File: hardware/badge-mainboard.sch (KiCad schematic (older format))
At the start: 0 parts

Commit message: splitted parts into connected schematic sheets
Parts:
- added C? (x2): 100nF, symbol C
- added C? (x3): 100nF, symbol C_Small
- added C?: 47uF, symbol C_Small
- added C?: 1uF, symbol C_Small
- added LED? (x3): WS2812b, WS2812B_1, symbol WS2812b
- added R? (x4): 10k, symbol R_Small
- added SW?: RESET-BTN, symbol SW_Push
- added U?: NINA-W102, symbol NINA-W102
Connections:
- net labels added: +1V8, +3.3V, +3V3, DTR, GND, NINA_SCL, NINA_SDA, RTS, RXD, TXD
- wire segments 0 -> 76
- no-connect marks 0 -> 1
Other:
- note added: "3 x RGBW LED Daisychain"
- note added: "Only one needed?\nVCC and VCC_IO are same in our case as we talk with 3.3v"
- note added: "Random I2C ports, any GPIO works."
- note added: "Random data port?"
- note added: "Which pullups? 10k or 200k?\nhttp://www.ti.com/lit/an/slva689/slva689.pdf"
- note added: "open drain buffers missing inthe picture for control signals (DTR & RTS)"

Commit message: Added NINA breakout module
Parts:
- removed C? (x2): 100nF, symbol C
- removed C?: 1uF, symbol C_Small
- removed R? (x2): 10k, symbol R_Small
- removed SW?: RESET-BTN, symbol SW_Push
- removed U?: NINA-W102, symbol NINA-W102
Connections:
- net labels removed: +3.3V, DTR, RTS
- wire segments 76 -> 52
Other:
- note added: "Random data port, can be changed if needed"
- note removed: "Only one needed?\nVCC and VCC_IO are same in our case as we talk with 3.3v"
- note removed: "Random data port?"
- note removed: "open drain buffers missing inthe picture for control signals (DTR & RTS)"

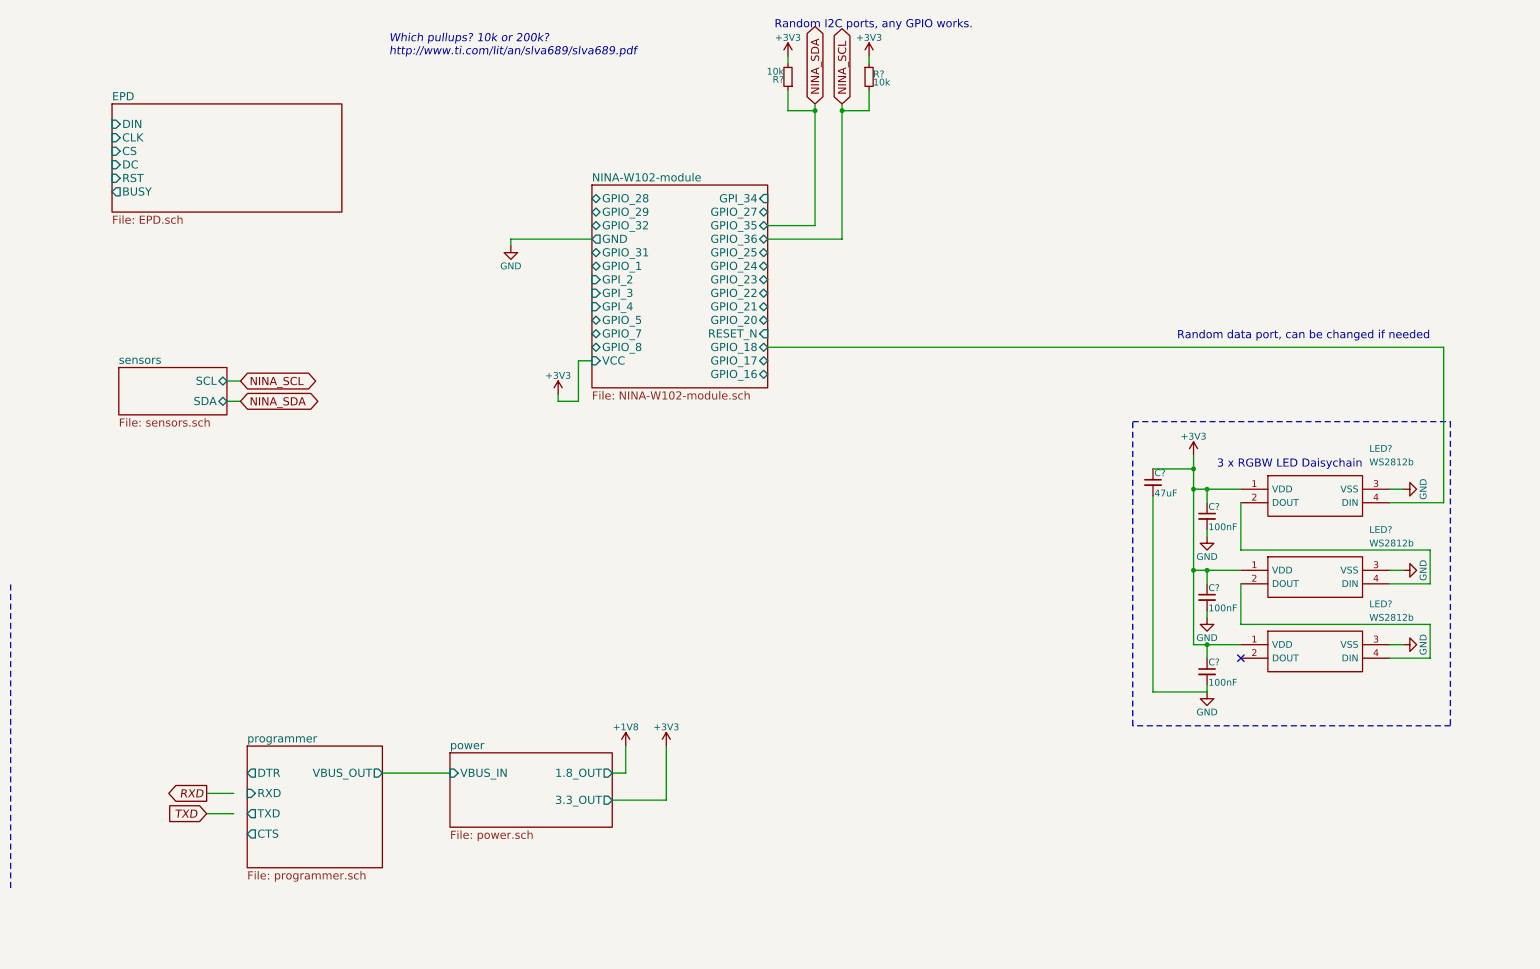
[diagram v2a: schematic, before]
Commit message: Added I2C headers and connected programmer to nina module
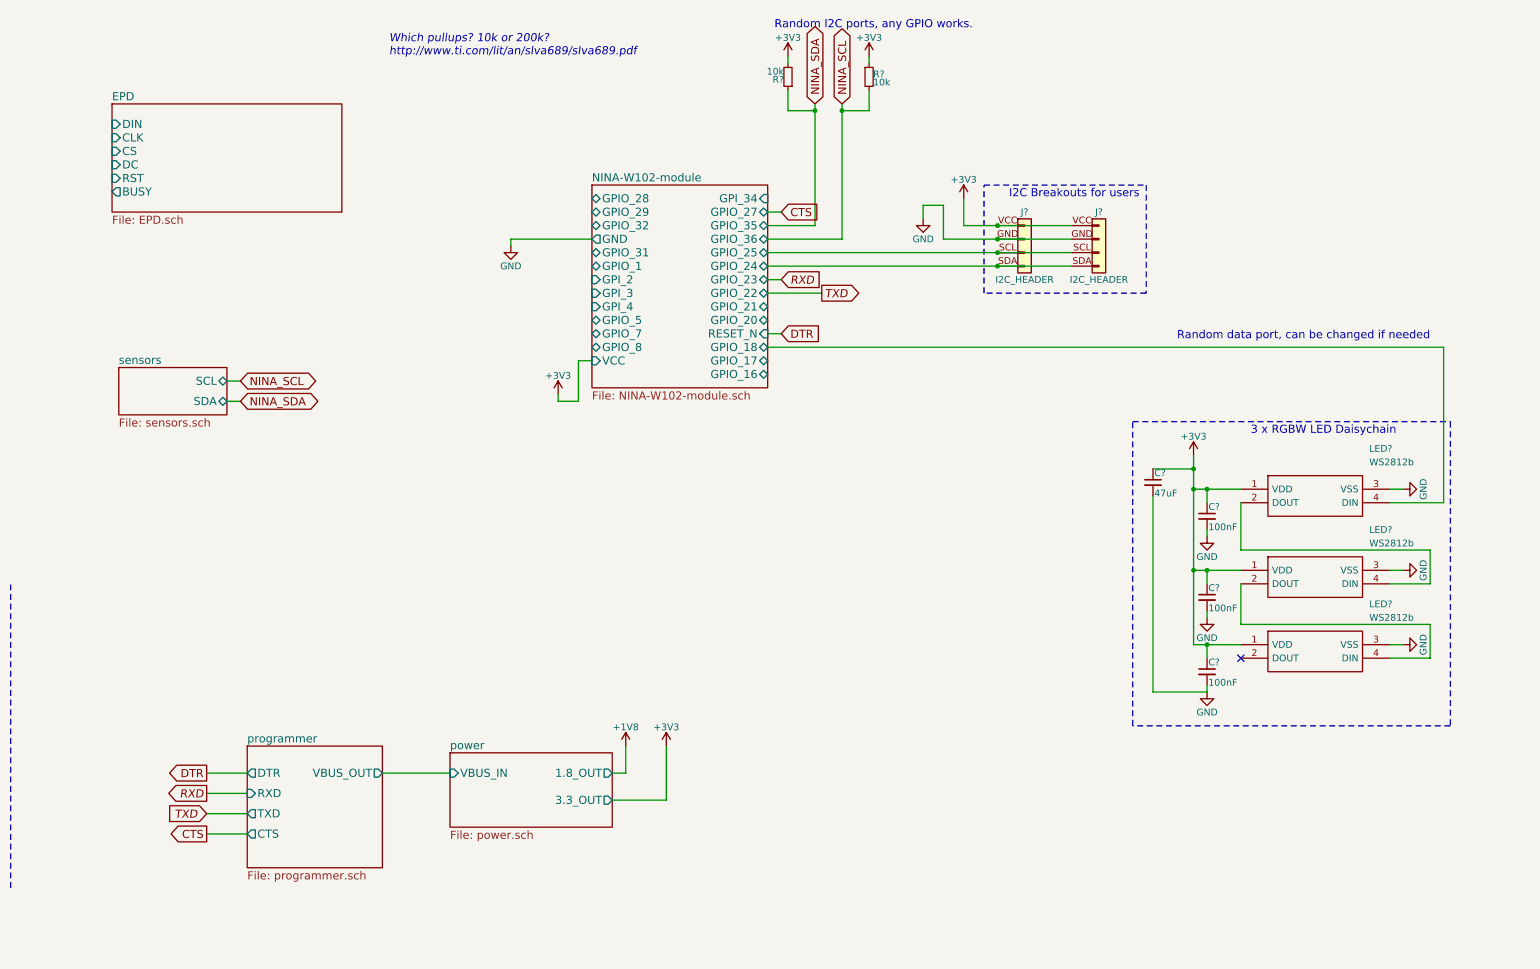
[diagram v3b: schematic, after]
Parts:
- added J? (x2): I2C_HEADER, symbol I2C_HEADER
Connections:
- net labels added: CTS, DTR
- wire segments 52 -> 66
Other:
- note added: "I2C Breakouts for users"
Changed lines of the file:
@@
 	1    0    0    -1
 $EndComp
-Text Notes 10500 3850 2    60   ~ 0
+Text Notes 10750 3600 2    60   ~ 0
 3 x RGBW LED Daisychain
 Text GLabel 6650 1150 1    60   BiDi ~ 0
@@
 Text Notes 3300 800  0    60   Italic 0
 Which pullups? 10k or 200k?\nhttp://www.ti.com/lit/an/slva689/slva689.pdf
-Wire Notes Line
-	500  6950 500  4700
-Wire Wire Line
-	9600 4100 9600 4450
-Wire Wire Line
-	9600 4450 11000 4450
-Wire Wire Line
-	11000 4450 11000 4700
-Wire Wire Line
-	11000 4700 10700 4700
-Wire Wire Line
-	9600 4700 9600 5000
-Wire Wire Line
-	9600 5000 11000 5000
-Wire Wire Line
-	10700 5250 11000 5250
-Wire Wire Line
-	10800 4600 10700 4600
-Wire Wire Line
-	10800 5150 10700 5150
-Wire Wire Line
-	10800 4000 10700 4000
-Wire Wire Line
-	11000 5250 11000 5000
-Wire Wire Line
-	9250 4000 9600 4000
-Wire Wire Line
-	9250 3750 9250 5150
-Wire Wire Line
-	9250 4600 9600 4600
-Connection ~ 9250 4000
-Wire Wire Line
-	9250 5150 9600 5150
-Connection ~ 9250 4600
-Wire Wire Line
-	9350 4300 9350 4350
-Wire Wire Line
-	9350 4100 9350 4000
-Connection ~ 9350 4000
-Wire Wire Line
-	9350 4900 9350 4950
-Wire Wire Line
-	9350 4700 9350 4600
-Wire Wire Line
-	9350 5450 9350 5500
-Wire Wire Line
-	9350 5250 9350 5150
-Connection ~ 9350 5150
-Connection ~ 9350 4600
-Wire Wire Line
-	11100 4100 10700 4100
-Wire Notes Line
-	8800 3500 11150 3500
-Wire Notes Line
-	11150 3500 11150 5750
-Wire Notes Line
-	11150 5750 8800 5750
-Wire Wire Line
-	6650 1150 6650 2150
-Wire Wire Line
-	6450 1150 6450 2050
-Wire Wire Line
-	8950 3850 9250 3850
-Connection ~ 9250 3850
-Wire Wire Line
-	8950 4050 8950 5500
-Wire Wire Line
-	8950 5500 9350 5500
-Wire Notes Line
-	8800 5750 8800 3500
-Connection ~ 6450 1200
 $Sheet
 S 1300 3100 800  350
@@
 Text GLabel 2200 3200 2    60   BiDi ~ 0
 NINA_SCL
-Wire Wire Line
-	2100 3200 2200 3200
-Wire Wire Line
-	2100 3350 2200 3350
 $Sheet
 S 2250 5900 1000 900
@@
 Text GLabel 1950 6250 0    60   Output Italic 0
 RXD
-Wire Wire Line
-	2150 6250 1950 6250
-Wire Wire Line
-	1950 6400 2150 6400
 $Sheet
 S 1250 1150 1700 800
@@
 F4 "3.3_OUT" O R 4950 6300 60
 $EndSheet
-Wire Wire Line
-	3250 6100 3750 6100
 $Comp
 L +1V8 #PWR08
@@
 	1    0    0    -1
 $EndComp
-Wire Wire Line
-	4950 6100 5050 6100
-Wire Wire Line
-	5050 6100 5050 5900
-Wire Wire Line
-	4950 6300 5350 6300
-Wire Wire Line
-	5350 6300 5350 5900
 $Comp
 L +3V3 #PWR010
@@
 	1    0    0    -1
 $EndComp
-Wire Wire Line
-	6450 1200 6250 1200
-Wire Wire Line
-	6250 1200 6250 1050
-Wire Wire Line
-	6250 850  6250 800
 $Comp
 L +3V3 #PWR011
@@
 	1    0    0    -1
 $EndComp
-Wire Wire Line
-	6850 800  6850 850
-Wire Wire Line
-	6850 1050 6850 1200
-Wire Wire Line
-	6850 1200 6650 1200
-Connection ~ 6650 1200
 $Comp
 L +3V3 #PWR012
@@
 F28 "GPIO_16" B R 6100 3150 60
 $EndSheet
-Wire Wire Line
-	6100 2950 11100 2950
-Wire Wire Line
-	11100 2950 11100 4100
-Wire Wire Line
-	6450 2050 6100 2050
-Wire Wire Line
-	6650 2150 6100 2150
 $Comp
 L +3V3 #PWR?
@@
 	1    0    0    -1
 $EndComp
-Wire Wire Line
-	4800 3050 4700 3050
-Wire Wire Line
-	4700 3050 4700 3350
-Wire Wire Line
-	4700 3350 4550 3350
-Wire Wire Line
-	4550 3350 4550 3300
 $Comp
 L GND #PWR?
@@
 	1    0    0    -1
 $EndComp
+$Comp
+L I2C_HEADER J?
+U 1 1 5AE74CFE
+P 8000 2150
+F 0 "J?" H 8000 2350 50  0000 C CNN
+F 1 "I2C_HEADER" H 8000 1850 50  0000 C CNN
+F 2 "" H 8000 2150 50  0001 C CNN
+F 3 "" H 8000 2150 50  0001 C CNN
+	1    8000 2150
+	1    0    0    -1
+$EndComp
+$Comp
+L I2C_HEADER J?
+U 1 1 5AE74E55
+P 8550 2150
+F 0 "J?" H 8550 2350 50  0000 C CNN
+F 1 "I2C_HEADER" H 8550 1850 50  0000 C CNN
+F 2 "" H 8550 2150 50  0001 C CNN
+F 3 "" H 8550 2150 50  0001 C CNN
+	1    8550 2150
+	1    0    0    -1
+$EndComp
+$Comp
+L +3V3 #PWR?
+U 1 1 5AE75A47
+P 7550 1850
+F 0 "#PWR?" H 7550 1700 50  0001 C CNN
+F 1 "+3V3" H 7550 1990 50  0000 C CNN
+F 2 "" H 7550 1850 50  0001 C CNN
+F 3 "" H 7550 1850 50  0001 C CNN
+	1    7550 1850
+	1    0    0    -1
+$EndComp
+$Comp
+L GND #PWR?
+U 1 1 5AE75B75
+P 7250 2000
+F 0 "#PWR?" H 7250 1750 50  0001 C CNN
+F 1 "GND" H 7250 1850 50  0000 C CNN
+F 2 "" H 7250 2000 50  0001 C CNN
+F 3 "" H 7250 2000 50  0001 C CNN
+	1    7250 2000
+	1    0    0    -1
+$EndComp
+Text Notes 8850 1850 2    60   ~ 0
+I2C Breakouts for users
+Text GLabel 1950 6550 0    60   Output ~ 0
+CTS
+Text GLabel 1950 6100 0    60   Output ~ 0
+DTR
+Wire Notes Line
+	500  6950 500  4700
+Wire Wire Line
+	9600 4100 9600 4450
+Wire Wire Line
+	9600 4450 11000 4450
+Wire Wire Line
+	11000 4450 11000 4700
+Wire Wire Line
+	11000 4700 10700 4700
+Wire Wire Line
+	9600 4700 9600 5000
+Wire Wire Line
+	9600 5000 11000 5000
+Wire Wire Line
+	10700 5250 11000 5250
+Wire Wire Line
+	10800 4600 10700 4600
+Wire Wire Line
+	10800 5150 10700 5150
+Wire Wire Line
+	10800 4000 10700 4000
+Wire Wire Line
+	11000 5250 11000 5000
+Wire Wire Line
+	9250 4000 9600 4000
+Wire Wire Line
+	9250 3750 9250 5150
+Wire Wire Line
+	9250 4600 9600 4600
+Connection ~ 9250 4000
+Wire Wire Line
+	9250 5150 9600 5150
+Connection ~ 9250 4600
+Wire Wire Line
+	9350 4300 9350 4350
+Wire Wire Line
+	9350 4100 9350 4000
+Connection ~ 9350 4000
+Wire Wire Line
+	9350 4900 9350 4950
+Wire Wire Line
+	9350 4700 9350 4600
+Wire Wire Line
+	9350 5450 9350 5500
+Wire Wire Line
+	9350 5250 9350 5150
+Connection ~ 9350 5150
+Connection ~ 9350 4600
+Wire Wire Line
+	11100 4100 10700 4100
+Wire Notes Line
+	8800 3500 11150 3500
+Wire Notes Line
+	11150 3500 11150 5750
+Wire Notes Line
+	11150 5750 8800 5750
+Wire Wire Line
+	6650 1150 6650 2150
+Wire Wire Line
+	6450 1150 6450 2050
+Wire Wire Line
+	8950 3850 9250 3850
+Connection ~ 9250 3850
+Wire Wire Line
+	8950 4050 8950 5500
+Wire Wire Line
+	8950 5500 9350 5500
+Wire Notes Line
+	8800 5750 8800 3500
+Connection ~ 6450 1200
+Wire Wire Line
+	2100 3200 2200 3200
+Wire Wire Line
+	2100 3350 2200 3350
+Wire Wire Line
+	1950 6250 2250 6250
+Wire Wire Line
+	1950 6400 2250 6400
+Wire Wire Line
+	3250 6100 3750 6100
+Wire Wire Line
+	4950 6100 5050 6100
+Wire Wire Line
+	5050 6100 5050 5900
+Wire Wire Line
+	4950 6300 5350 6300
+Wire Wire Line
+	5350 6300 5350 5900
+Wire Wire Line
+	6450 1200 6250 1200
+Wire Wire Line
+	6250 1200 6250 1050
+Wire Wire Line
+	6250 850  6250 800
+Wire Wire Line
+	6850 800  6850 850
+Wire Wire Line
+	6850 1050 6850 1200
+Wire Wire Line
+	6850 1200 6650 1200
+Connection ~ 6650 1200
+Wire Wire Line
+	6100 2950 11100 2950
+Wire Wire Line
+	11100 2950 11100 4100
+Wire Wire Line
+	6450 2050 6100 2050
+Wire Wire Line
+	6650 2150 6100 2150
+Wire Wire Line
+	4800 3050 4700 3050
+Wire Wire Line
+	4700 3050 4700 3350
+Wire Wire Line
+	4700 3350 4550 3350
+Wire Wire Line
+	4550 3350 4550 3300
 Wire Wire Line
 	4800 2150 4200 2150
 Wire Wire Line
 	4200 2150 4200 2200
+Wire Wire Line
+	6100 2250 8350 2250
+Wire Wire Line
+	6100 2350 8350 2350
+Connection ~ 7800 2350
+Connection ~ 7800 2250
+Wire Wire Line
+	7550 2050 8350 2050
+Wire Wire Line
+	7550 2050 7550 1850
+Wire Wire Line
+	7400 2150 8350 2150
+Wire Wire Line
+	7400 2150 7400 1900
+Wire Wire Line
+	7400 1900 7250 1900
+Wire Wire Line
+	7250 1900 7250 2000
+Connection ~ 7800 2150
+Connection ~ 7800 2050
+Wire Notes Line
+	7700 2550 7700 1750
+Wire Notes Line
+	7700 1750 8900 1750
+Wire Notes Line
+	8900 1750 8900 2550
+Wire Notes Line
+	8900 2550 7700 2550
+Wire Wire Line
+	1950 6100 2250 6100
+Wire Wire Line
+	2250 6550 1950 6550
+Text GLabel 6500 2550 2    60   Output Italic 0
+TXD
+Text GLabel 6200 2450 2    60   Input Italic 0
+RXD
+Text GLabel 6200 1950 2    60   Input ~ 0
+CTS
+Text GLabel 6200 2850 2    60   Input ~ 0
+DTR
+Wire Wire Line
+	6200 1950 6100 1950
+Wire Wire Line
+	6200 2850 6100 2850
+Wire Wire Line
+	6200 2450 6100 2450
+Wire Wire Line
+	6500 2550 6100 2550
 $EndSCHEMATC

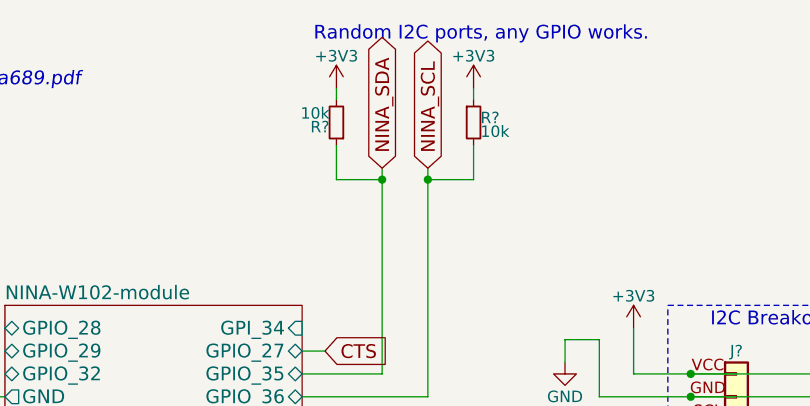
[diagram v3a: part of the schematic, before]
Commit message: Changed pullups for i2c to 4.7k
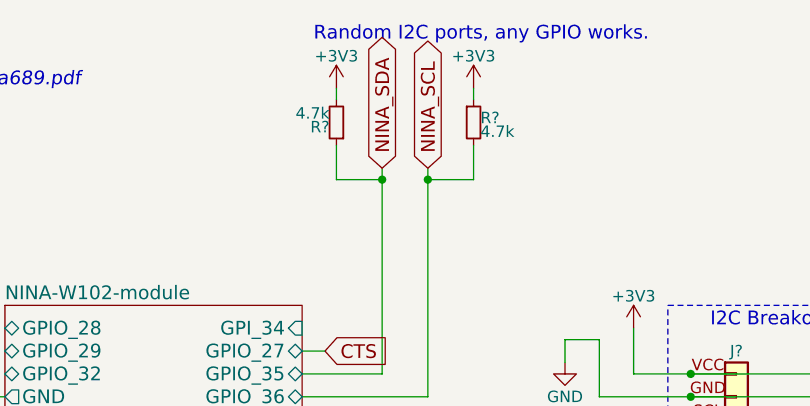
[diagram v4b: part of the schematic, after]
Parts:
- R? (x2): value 10k -> 4.7k
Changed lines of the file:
@@
 P 6250 950
 F 0 "R?" H 6280 970 50  0000 L CNN
-F 1 "10k" H 6280 910 50  0000 L CNN
+F 1 "4.7k" H 6280 910 50  0000 L CNN
 F 2 "" H 6250 950 50  0001 C CNN
 F 3 "" H 6250 950 50  0001 C CNN
@@
 P 6850 950
 F 0 "R?" H 6880 970 50  0000 L CNN
-F 1 "10k" H 6880 910 50  0000 L CNN
+F 1 "4.7k" H 6880 910 50  0000 L CNN
 F 2 "" H 6850 950 50  0001 C CNN
 F 3 "" H 6850 950 50  0001 C CNN
